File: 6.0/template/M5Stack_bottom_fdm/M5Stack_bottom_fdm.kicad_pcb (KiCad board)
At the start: 2 copper layers, 50 x 50 mm, 9 parts, among them U1 M-BUS

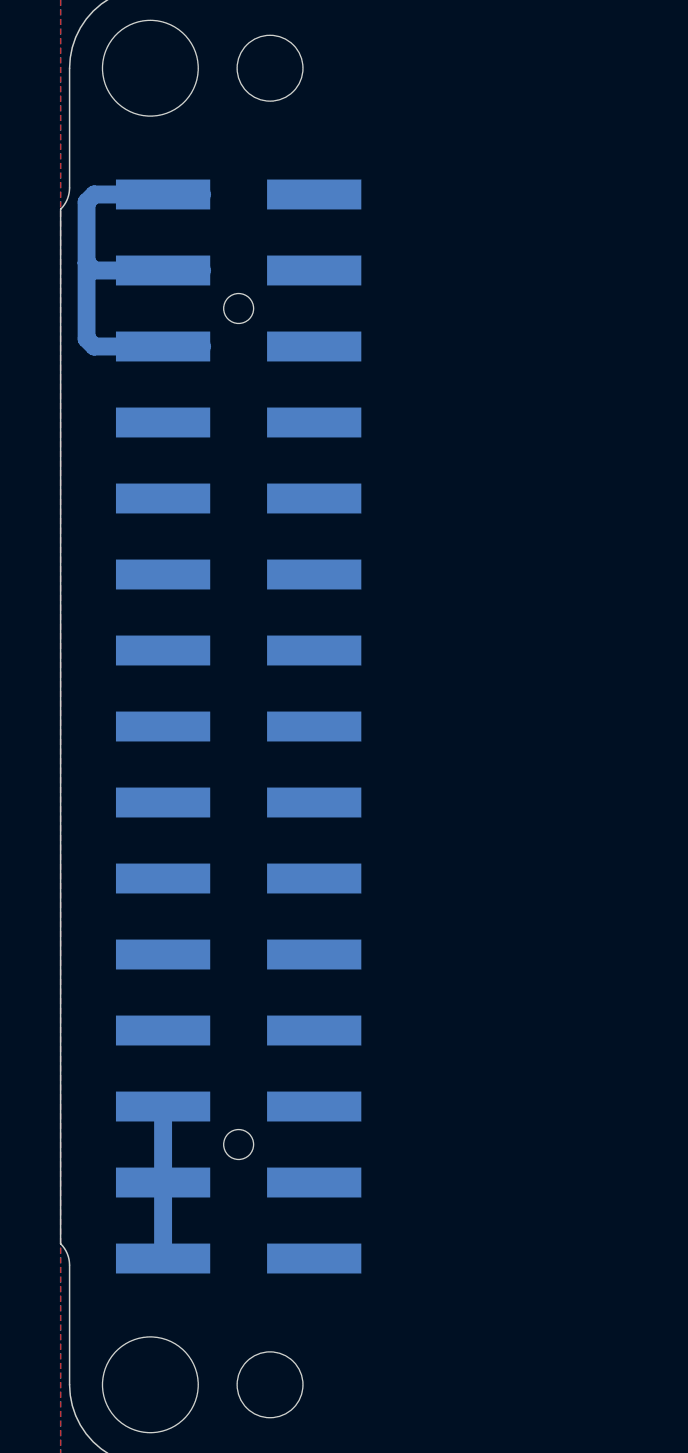
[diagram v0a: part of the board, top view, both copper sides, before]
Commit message: template M5Stack
M-BUS connector  U1 to J1
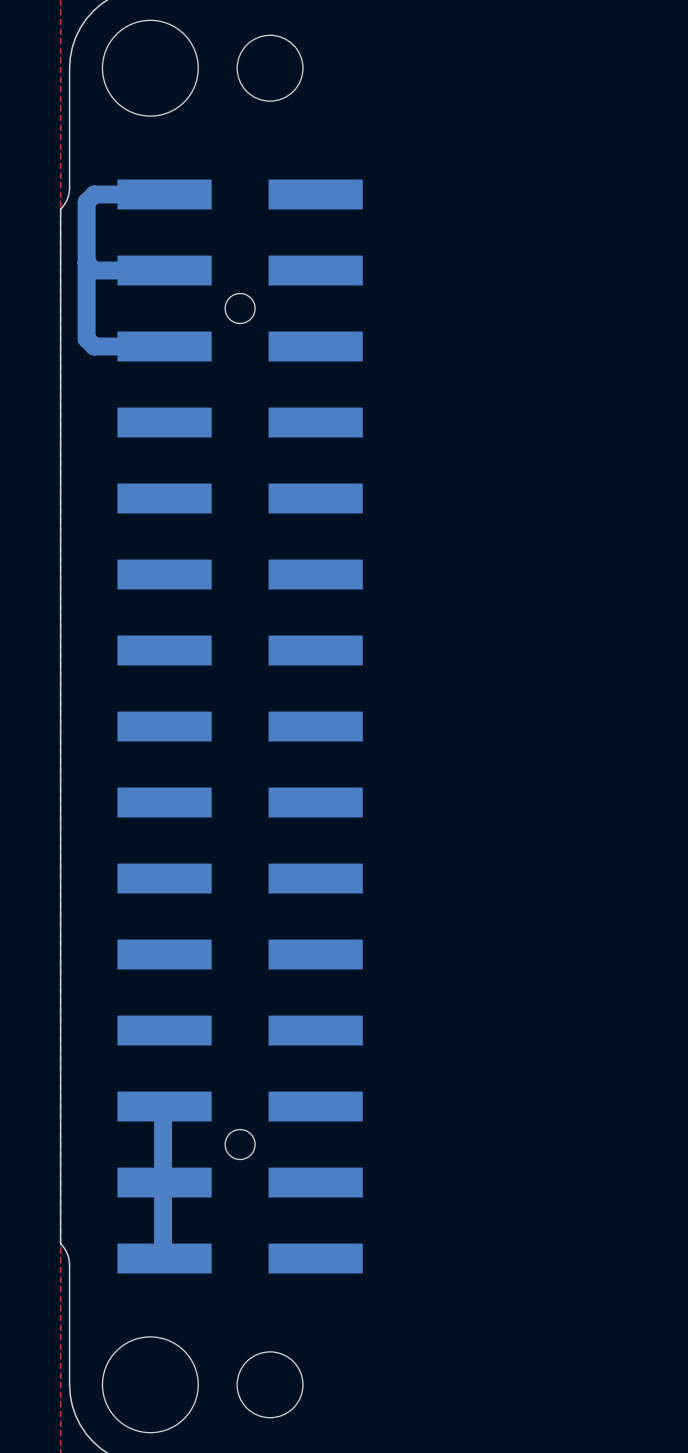
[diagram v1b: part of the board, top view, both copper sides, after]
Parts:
- removed U1: M-BUS, @bf:BF@M5Stack_MBUS_Headder
- added J1: M-BUS, @bf:BF@M5Stack_MBUS_Headder, F.Cu at (108.0, 127.0)
